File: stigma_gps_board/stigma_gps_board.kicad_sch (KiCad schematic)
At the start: 18 parts, among them J1 DF40GB-70DP-0.4V, U1 NCP115AMX120TCG, U2 SAM-M10Q

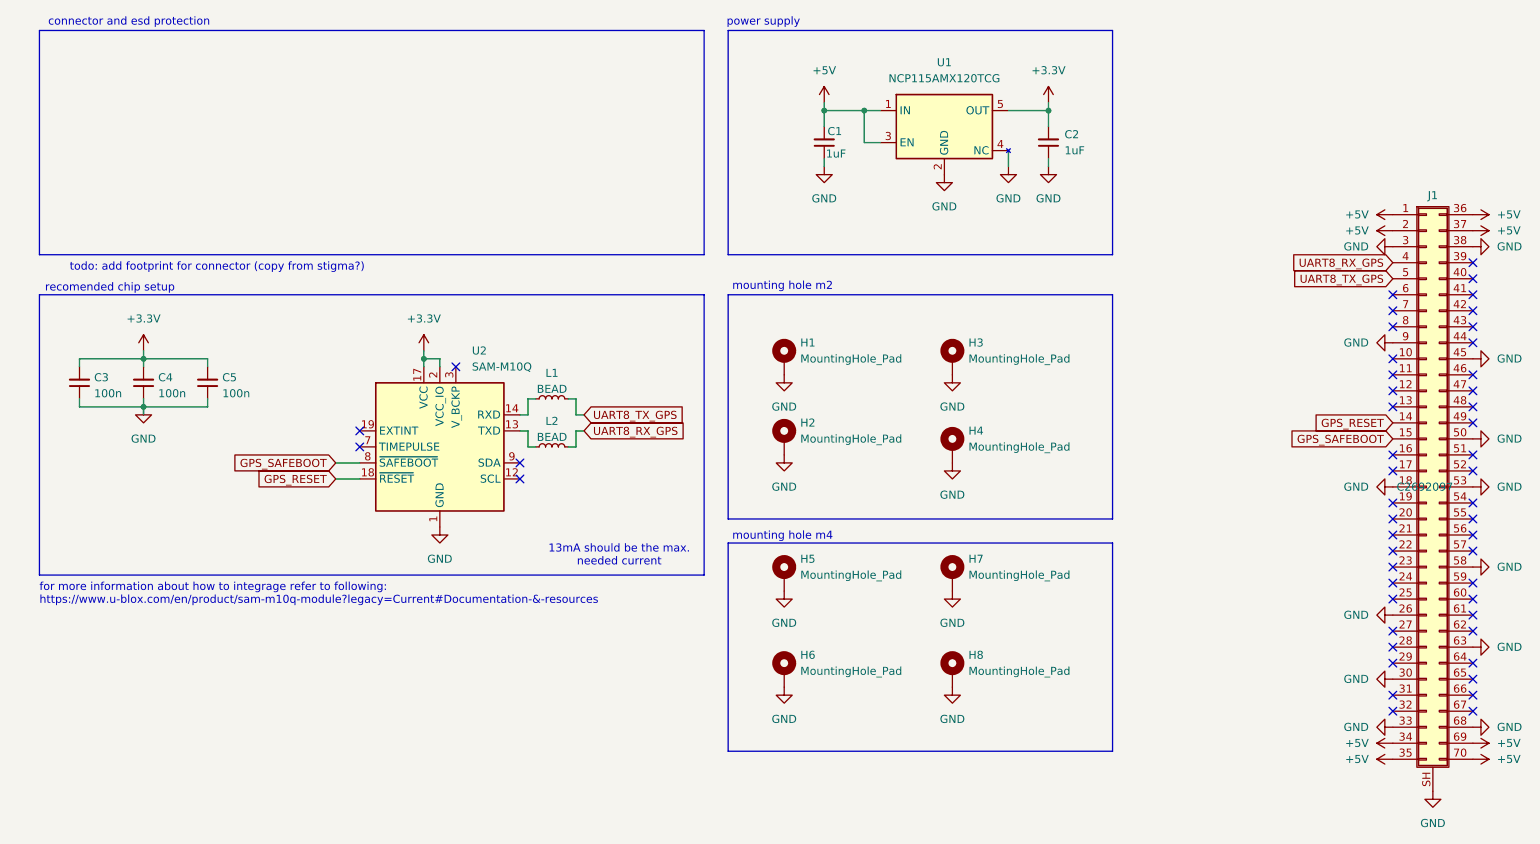
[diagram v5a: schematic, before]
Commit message: some lcsc number changes
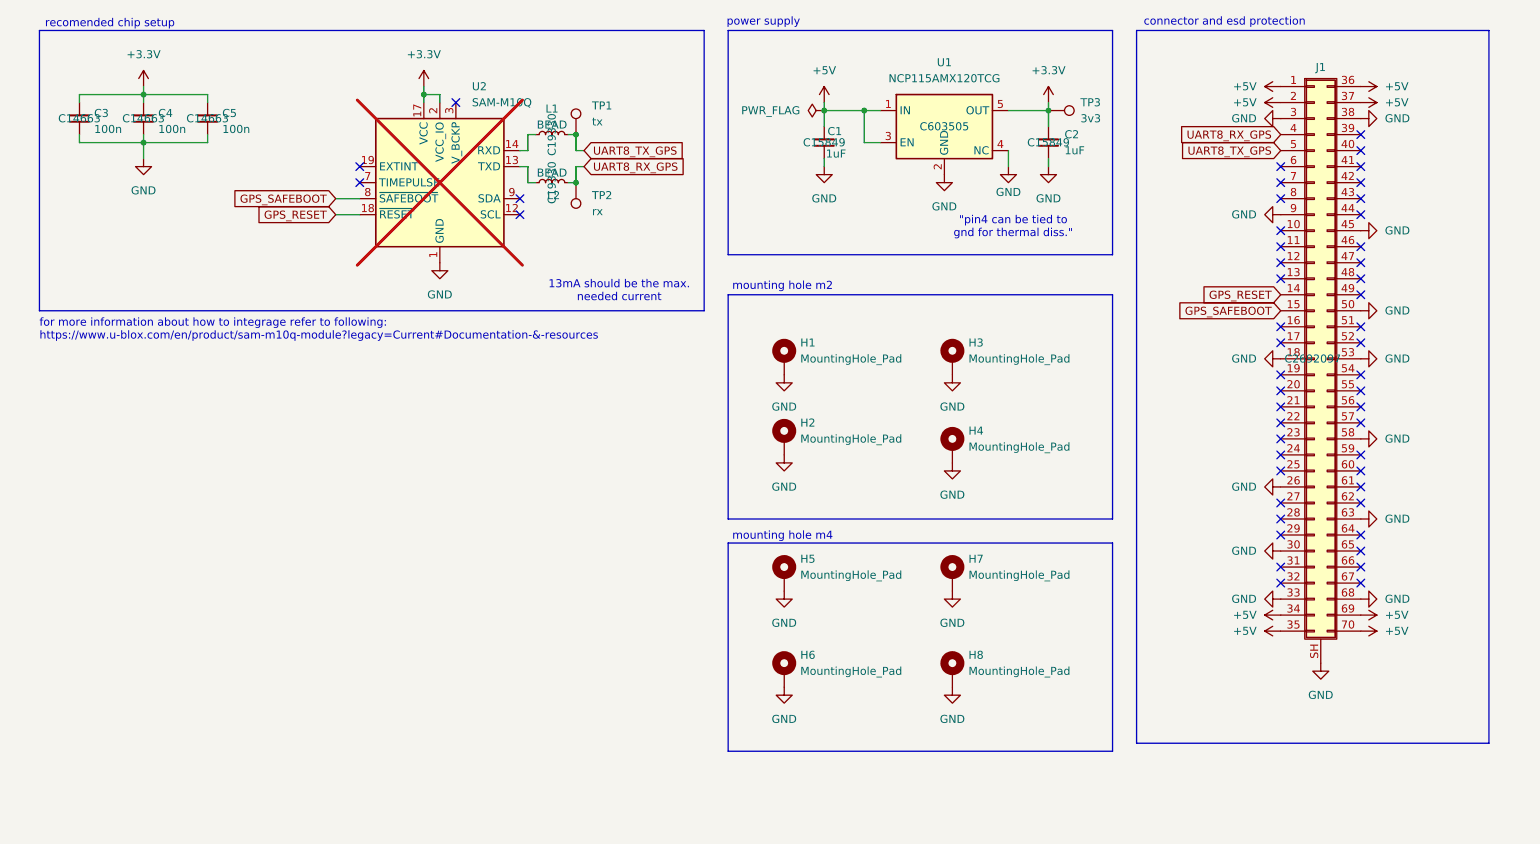
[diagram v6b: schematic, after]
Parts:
- added TP1: tx, TestPoint:TestPoint_Pad_D1.5mm, symbol Connector:TestPoint
- added TP2: rx, TestPoint:TestPoint_Pad_D1.5mm, symbol Connector:TestPoint
- added TP3: 3v3, TestPoint:TestPoint_Pad_D1.5mm, symbol Connector:TestPoint
- C1, C2: LCSC (none) -> C15849; LCSC# C1591 -> (none)
- C3, C4, C5: LCSC (none) -> C14663; LCSC# C1591 -> (none)
- L1, L2: LCSC (none) -> C19330; LCSC# C19330 -> (none)
- U2: now not fitted
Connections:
- net +3.3V: now also TP3.1
- net UART8_RX_GPS: now also TP2.1
- net UART8_TX_GPS: now also TP1.1
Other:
- note added: ""pin4 can be tied to gnd for thermal diss.""
- note removed: "todo: add footprint for connector (copy from stigma?)"
- moved on the sheet: C3, C4, C5, J1, L1, L2
